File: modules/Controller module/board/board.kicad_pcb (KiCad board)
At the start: 2 copper layers, 60 parts, among them IC1 DW01A, J1 USB_C_Receptacle, J2 Conn_01x05_Female, J3 Conn_01x03_Female, J4 Conn_01x04_Female, J5 Conn_02x12_Odd_Even, J6 Conn_01x06_Female, J7 Conn_01x02_Female, J8 Conn_01x08_Female, Q1 AO3400A, Q2 AO3401A, Q3 FS8205A, SW1 SW_Push, SW2 SW_Push, U1 HT7833, U2 ESP32-WROOM-32D, U3 TP4056, U4 MPU-6050

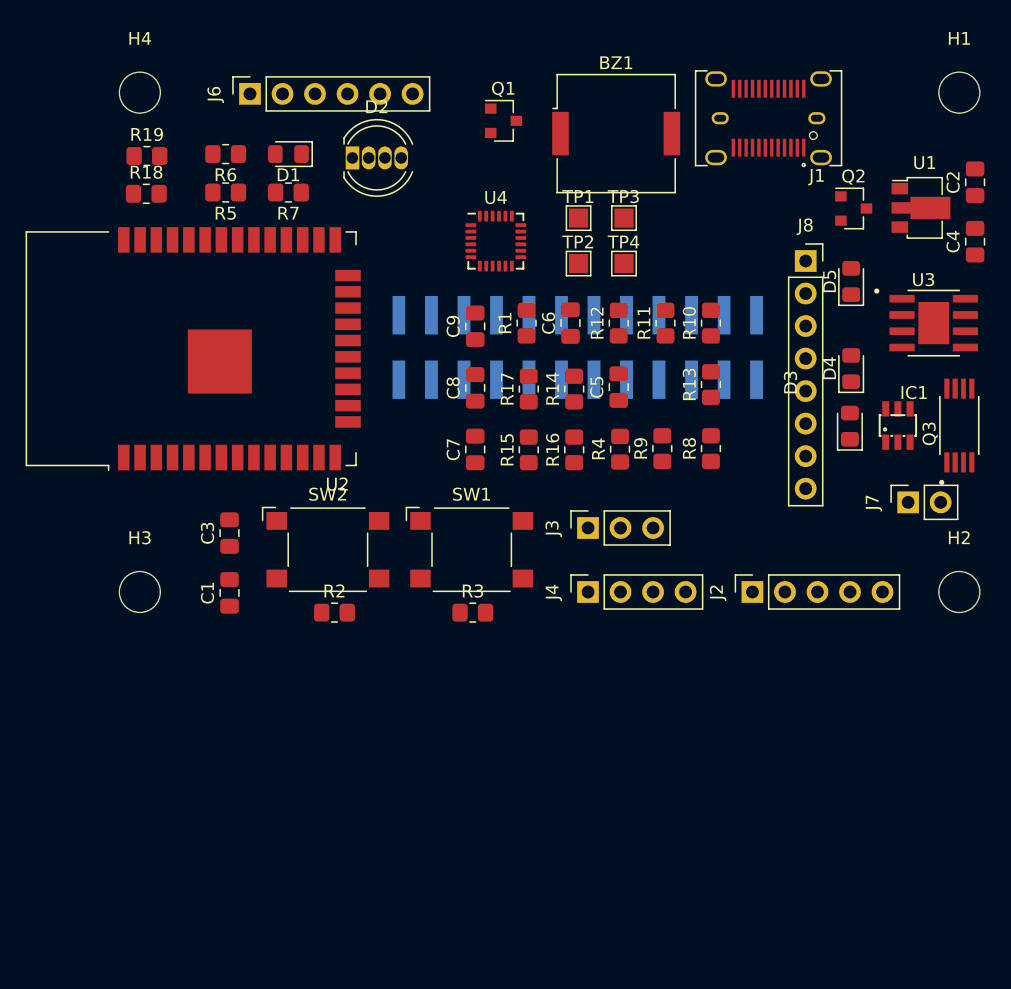
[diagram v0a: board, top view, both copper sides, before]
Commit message: Controller module: Schematic and PCB layout
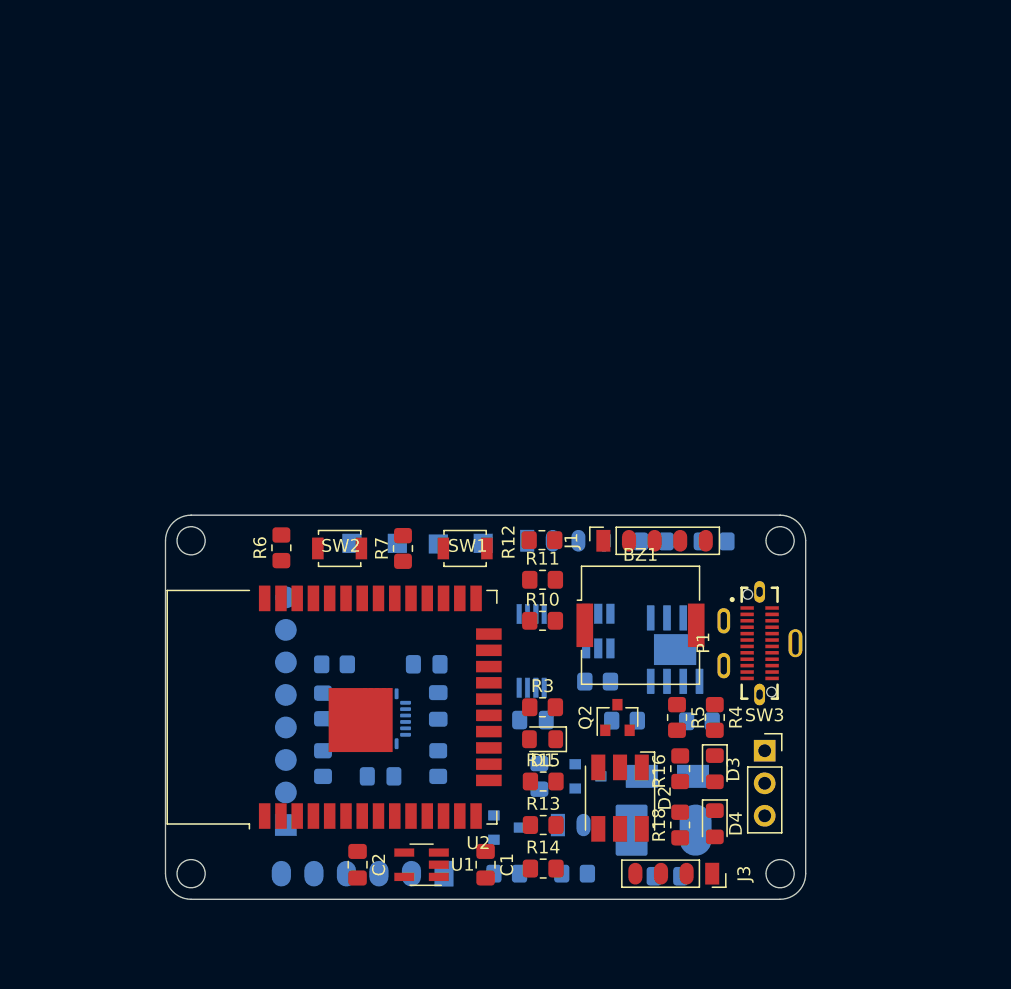
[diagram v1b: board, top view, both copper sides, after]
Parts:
- removed the C1 at (110.0, 92.1)
- removed the C3 at (110.0, 87.4)
- removed the J1 at (152.1, 55.0)
- removed the J3 at (138.0, 87.0)
- removed the J5 at (137.2, 72.9)
- added J2: Conn_01x04_Female, Board:SolderWire_1x04_P2.00mm, B.Cu at (133.2, 88.0)
- added J4: Conn_01x02, Board:SolderWire_1x02_P2.00mm, B.Cu at (135.7, 110.2)
- added P1: USB_C_Plug_USB2.0, Board:GCT_USB4151-GF-C_REVA, F.Cu at (151.4, 96.0)
- added Q2: AO3400A, Package_TO_SOT_SMD:SOT-23, F.Cu at (140.3, 101.8)
- added R1: 10k, Resistor_SMD:R_0805_2012Metric_Pad1.20x1.40mm_HandSolder, B.Cu at (143.1, 88.0)
- added R2: 10k, Resistor_SMD:R_0805_2012Metric_Pad1.20x1.40mm_HandSolder, B.Cu at (147.8, 88.0)
- added R4: 100R, Resistor_SMD:R_0805_2012Metric_Pad1.20x1.40mm_HandSolder, F.Cu at (147.9, 101.8)
- added R5: 10k, Resistor_SMD:R_0805_2012Metric_Pad1.20x1.40mm_HandSolder, F.Cu at (144.9, 101.8)
- added R8: 100R, Resistor_SMD:R_0805_2012Metric_Pad1.20x1.40mm_HandSolder, B.Cu at (136.9, 114.0)
- added R9: 10k, Resistor_SMD:R_0805_2012Metric_Pad1.20x1.40mm_HandSolder, B.Cu at (131.7, 114.0)
- added SW3: SW_SPST, Connector_PinSocket_2.54mm:PinSocket_1x03_P2.54mm_Vertical, F.Cu at (151.8, 104.4)
- C1: renamed from C2; value 1uF -> 10uF
- C2: renamed from C4; value 2.2uF -> 10uF
- C3: renamed from C5; moved to B.Cu
- C4: renamed from C6; moved to B.Cu
- C5: renamed from C7; moved to B.Cu
- C6: renamed from C8; moved to B.Cu
- C7: renamed from C9; moved to B.Cu
- D2: value LED_RGBC -> LED_RGB; footprint LED_THT:LED_D5.0mm-4_RGB -> LED_SMD:LED_RGB_5050-6
- D5: footprint Diode_SMD:D_0805_2012Metric_Pad1.15x1.40mm_HandSolder -> Diode_SMD:D_SMA; moved to B.Cu
- H1, H2, H3, H4: footprint MountingHole:MountingHole_3.2mm_M3 -> MountingHole:MountingHole_2.2mm_M2
- IC1: footprint board:SOT23-6 -> Package_TO_SOT_SMD:SOT-23-6_Handsoldering; moved to B.Cu
- J1: renamed from J2; footprint Connector_PinSocket_2.54mm:PinSocket_1x05_P2.54mm_Vertical -> Board:SolderWire_1x05_P2.00mm
- J3: renamed from J4; footprint Connector_PinSocket_2.54mm:PinSocket_1x04_P2.54mm_Vertical -> Board:SolderWire_1x04_P2.00mm
- J5: renamed from J6; footprint Connector_PinSocket_2.54mm:PinSocket_1x06_P2.54mm_Vertical -> Board:SolderWire_1x06_P2.54mm; moved to B.Cu
- J6: renamed from J7; footprint Connector_PinSocket_2.54mm:PinSocket_1x02_P2.54mm_Vertical -> Board:SolderWire-SMD-BATT; moved to B.Cu
- J7: renamed from J8; footprint Connector_PinSocket_2.54mm:PinSocket_1x08_P2.54mm_Vertical -> Board:MPU6050_Breakout; moved to B.Cu
- Q1, TP1, TP2, TP3, TP4, U4: moved to B.Cu
- Q3: renamed from Q2; moved to B.Cu
- Q4: renamed from Q3; footprint board:SOP65P640X120-8N -> Board:SOP65P640X120-8N; moved to B.Cu
- R17: renamed from R9; moved to B.Cu
- R19: renamed from R11; moved to B.Cu
- R20: renamed from R12; moved to B.Cu
- R21: renamed from R13; moved to B.Cu
- R22: renamed from R14; moved to B.Cu
- R23: renamed from R15; moved to B.Cu
- R24: renamed from R16; moved to B.Cu
- R25: renamed from R17; moved to B.Cu
- SW1, SW2: footprint Button_Switch_SMD:SW_SPST_Omron_B3FS-100xP -> Button_Switch_SMD:SW_SPST_B3U-1000P
- U1: value HT7833 -> ME6211; footprint Package_TO_SOT_SMD:SOT-89-3 -> Package_TO_SOT_SMD:SOT-23-5_HandSoldering
- U3: footprint board:SOP127P600X175-9N -> Board:SOP127P600X175-9N; moved to B.Cu
- moved C2 68.5 mm to (120.0, 113.3), turned to 270 degrees
- moved C1 65.6 mm to (130.0, 113.3), turned to 270 degrees
- moved U1 64.4 mm to (125.0, 113.3), turned to 180 degrees
- moved J5 62.8 mm to (126.8, 114.0)
- moved R14 61.1 mm to (134.5, 113.6), turned to 0 degrees
- moved J7 59.7 mm to (114.5, 110.0)
- moved R13 55.3 mm to (134.5, 110.2), turned to 0 degrees
- moved Q1 55.2 mm to (131.7, 110.4)
- moved D2 54.2 mm to (140.5, 108.1), turned to 270 degrees
- moved R15 50.1 mm to (134.5, 106.8), turned to 0 degrees
- moved D1 49.8 mm to (134.4, 103.5)
- moved Q3 49.0 mm to (138.0, 106.4)
- moved C4 43.9 mm to (144.2, 114.2), turned to 0 degrees
- moved R11 43.2 mm to (134.4, 91.0)
- moved R12 43.0 mm to (134.4, 88.0)
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- renumbered R4 to R10, R18 to R11, R19 to R12, R5 to R13, R6 to R14, R7 to R15, R8 to R16, R10 to R18, R1 to R3, R2 to R6, R3 to R7
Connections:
- C1 pad 2: Net-(C2-Pad2) -> GND
- C2 pad 2: Net-(C2-Pad2) -> GND
- D2 pad 1: Net-(D2-Pad1) -> GND
- D2 pad 2: Net-(D2-Pad2) -> GND
- D2 pad 3: Net-(D2-Pad3) -> GND
- D2 pad 4: GND -> Net-(D2-Pad4)
- Q1 pad 1: /BUZZER -> Net-(Q1-Pad1)
- R13 pad 2: Net-(D2-Pad3) -> Net-(D2-Pad4)
- R14 pad 2: Net-(D2-Pad2) -> Net-(D2-Pad5)
- R15 pad 2: Net-(D2-Pad1) -> Net-(D2-Pad6)
- U1 pad 1: GND -> VCC
- U1 pad 2: VCC -> GND
- U1 pad 3: +3V3 -> VCC
- U2 pad 23: /IO15 -> (no net)
- U2 pad 29: /IO5 -> (no net)
- U2 pad 37: /IO23 -> /BTN-C
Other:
- board outline added: 50 x 30 mm

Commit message: Controller module: PCB complete
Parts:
- removed TP1, TP2, TP3, TP4: TestPoint, TestPoint:TestPoint_Pad_1.5x1.5mm
- added D2: LED, LED_SMD:LED_0805_2012Metric_Pad1.15x1.40mm_HandSolder, F.Cu at (130.0, 113.2)
- added R6: 10k, Resistor_SMD:R_0805_2012Metric_Pad1.20x1.40mm_HandSolder, F.Cu at (127.3, 113.2)
- J6: footprint Board:SolderWire-SMD-BATT -> Board:SolderWire_1x02_P2.00mm
- U2: footprint RF_Module:ESP32-WROOM-32 -> Board:ESP32-WROOM-32
- moved C4 23.4 mm to (144.7, 90.8)
- moved R1 23.1 mm to (120.0, 88.2)
- moved R2 23.1 mm to (124.8, 88.2)
- moved J6 23.0 mm to (145.7, 88.0), turned to 90 degrees
- moved R3 17.3 mm to (122.2, 113.2), turned to 90 degrees
- moved C1 16.5 mm to (134.5, 97.4), turned to 0 degrees
- moved C2 16.4 mm to (134.5, 105.7), turned to 0 degrees
- moved U1 15.1 mm to (134.5, 101.6), turned to 270 degrees
- moved D1 13.8 mm to (124.7, 113.2), turned to 270 degrees
- moved R10 11.9 mm to (143.4, 112.0), turned to 90 degrees
- moved R9 9.46 mm to (146.2, 112.0), turned to 270 degrees
- moved Q1 8.11 mm to (139.6, 112.0), turned to 180 degrees
- moved J4 2.11 mm to (135.8, 112.3), turned to 90 degrees
- moved R20 2.10 mm to (138.8, 102.0)
- moved R16 2.00 mm to (134.5, 108.8)
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- renumbered D2 to D3, D3 to D4, D4 to D5, D5 to D6, R9 to R10, R10 to R11, R11 to R12, R12 to R13, R13 to R14, R14 to R15, R15 to R16, R16 to R17, R17 to R18, R18 to R19, R19 to R20, R20 to R21, R21 to R22, R22 to R23, R23 to R24, R24 to R25, R25 to R26, R6 to R7, R7 to R8, R8 to R9, SW3 to SW2, SW2 to SW3
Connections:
- J7 pad 1: +3V3 -> VCC
- U2 pad 23: (no net) -> /IO15
- U2 pad 29: (no net) -> /IO15
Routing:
- net GND: track 0.00 -> 267.3 mm, vias 0 -> 12
- net +3V3: track 0.00 -> 153.9 mm, vias 0 -> 4
- net +5V: track 0.00 -> 70.2 mm, vias 0 -> 1
- net VCC: track 0.00 -> 64.0 mm, vias 0 -> 1
- net /IO16: track 0.00 -> 61.4 mm, vias 0 -> 1
- net /IO15: track 0.00 -> 60.4 mm, vias 0 -> 2
- net /BUZZER: track 0.00 -> 52.8 mm, vias 0 -> 2
- net /BTN2: track 0.00 -> 50.9 mm, vias 0 -> 3
- net /EN: track 0.00 -> 47.1 mm, vias 0 -> 2
- net /BTN1: track 0.00 -> 45.1 mm, vias 0 -> 2
- net /TX: track 0.00 -> 43.9 mm, vias 0 -> 1
- net /BTN-C: track 0.00 -> 41.4 mm, vias 0 -> 1
- net /BTN4: track 0.00 -> 37.9 mm, vias 0 -> 2
- net /BTN3: track 0.00 -> 35.9 mm, vias 0 -> 2
- net Net-(BZ1-Pad1): track 0.00 -> 35.3 mm, vias 0 -> 1
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- added copper zone on B.Cu, net GND
- added copper zone on F.Cu, net GND
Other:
- net class Default: trace_width 0.25 -> 0.2

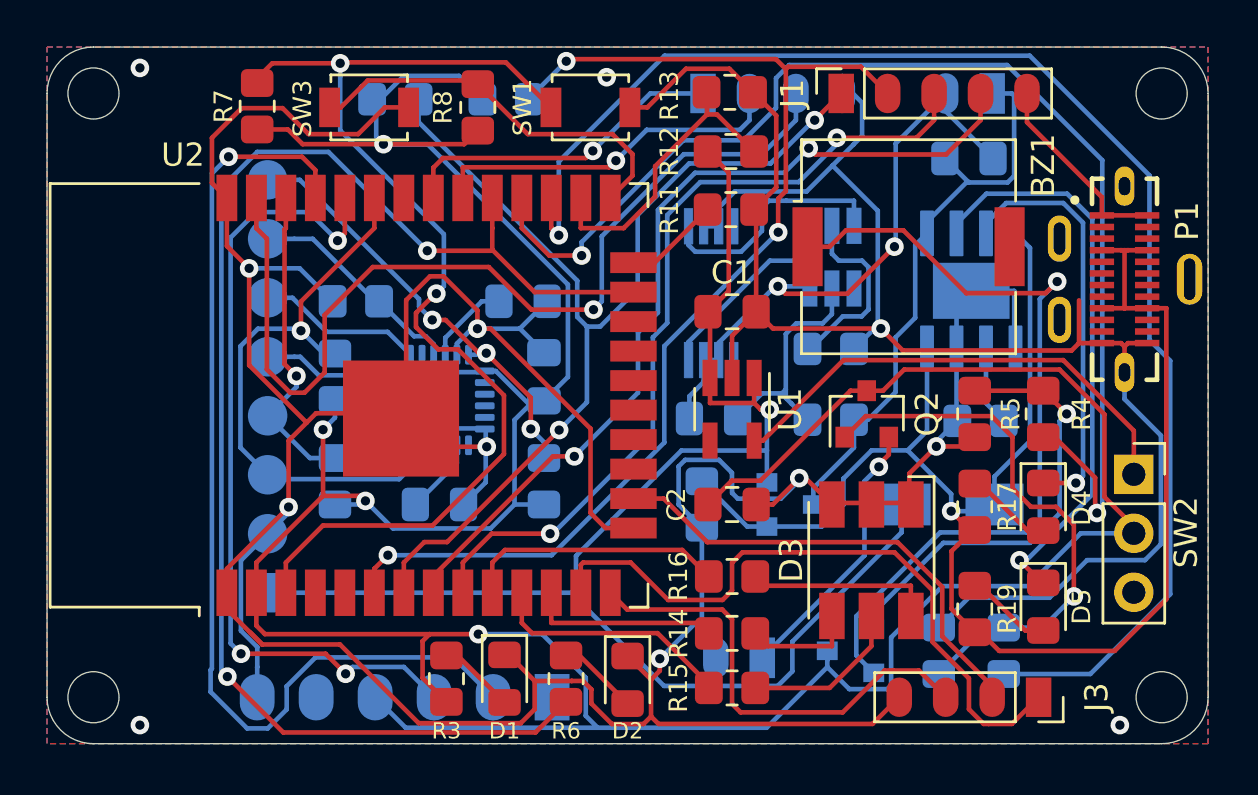
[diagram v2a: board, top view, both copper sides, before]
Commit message: Controller module: PCB modular
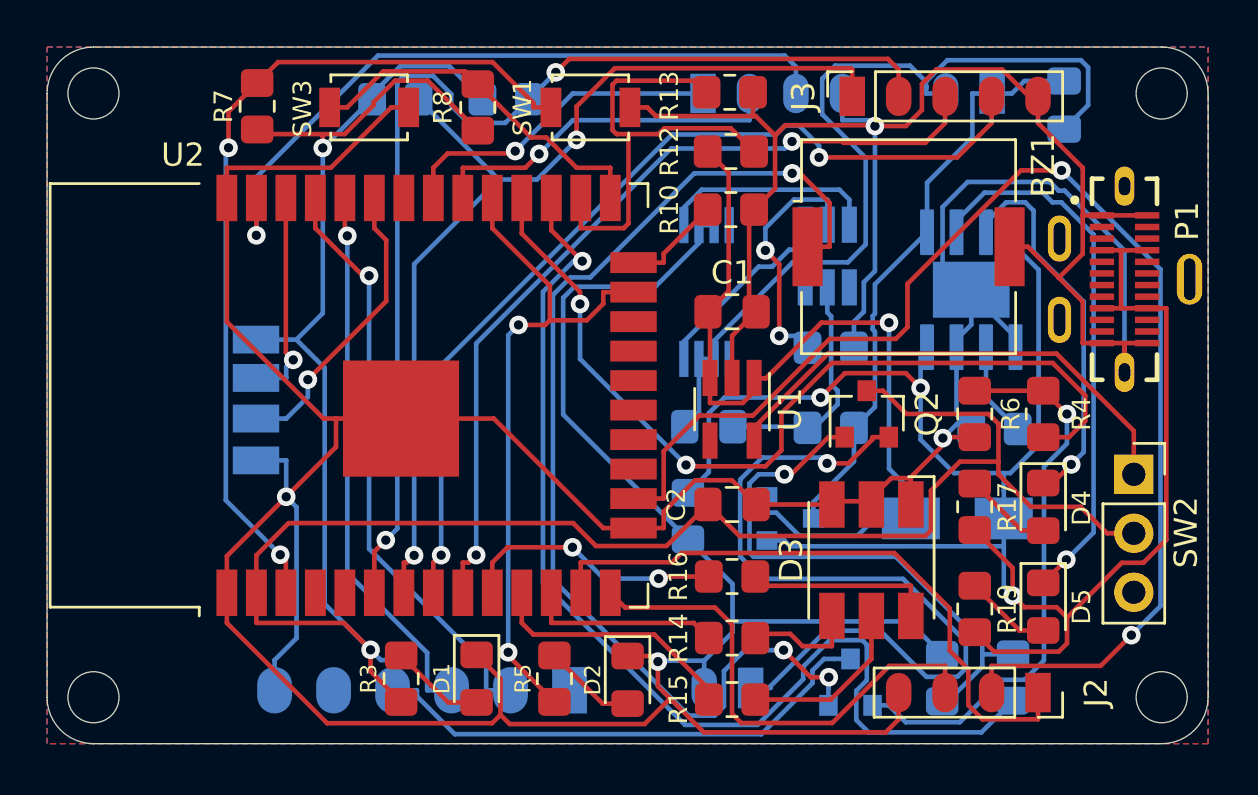
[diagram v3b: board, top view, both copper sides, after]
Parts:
- removed C5, C6: 0.1uF, Capacitor_SMD:C_0805_2012Metric_Pad1.18x1.45mm_HandSolder
- removed C7: 2.2nF, Capacitor_SMD:C_0805_2012Metric_Pad1.18x1.45mm_HandSolder
- removed J7: Conn_01x08_Female, Board:MPU6050_Breakout
- removed R23, R25, R26: 10k, Resistor_SMD:R_0805_2012Metric_Pad1.20x1.40mm_HandSolder
- removed R24: 4.7k, Resistor_SMD:R_0805_2012Metric_Pad1.20x1.40mm_HandSolder
- removed the U4 at (121.9, 101.2)
- added U3: Inertial_Measurement_Unit, Board:Inertial_Measurement_Unit_Board, B.Cu at (121.5, 101.1)
- moved C4 4.70 mm to (148.8, 88.5), turned to 270 degrees
- moved R3 1.95 mm to (120.2, 113.2)
- moved J4 1.39 mm to (135.3, 113.6)
- moved Q1 1.35 mm to (139.6, 113.3), turned to 90 degrees
- moved R9 1.22 mm to (146.6, 113.2)
- moved D1 1.20 mm to (123.5, 113.2)
- moved R11 1.18 mm to (143.6, 113.2)
- moved J5 0.81 mm to (127.5, 113.7)
- moved R18 0.78 mm to (132.6, 106.2)
- moved D6 0.72 mm to (144.2, 106.3)
- moved R20 0.69 mm to (145.8, 102.5)
- moved Q3 0.60 mm to (137.0, 106.3)
- moved R15 0.50 mm to (134.5, 114.1)
- moved R5 0.50 mm to (126.8, 113.2)
- moved J3 0.49 mm to (139.7, 88.1)
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- renumbered J2 to J1, J3 to J2, J1 to J3, R11 to R10, R10 to R11, R21 to R20, R20 to R21, R6 to R5, R5 to R6, U3 to U4
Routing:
- net /BTN-M: track 21.2 -> 56.6 mm, vias 0 -> 2
- net /IO15: track 60.4 -> 29.4 mm
- net VCC: track 64.0 -> 37.5 mm
- net Net-(J4-Pad1): track 11.8 -> 34.4 mm
- net +3V3: track 153.9 -> 134.0 mm, vias 4 -> 2
- net /IMU/INT: track 19.0 -> 0.00 mm, vias 3 -> 0
- net /TX: track 43.9 -> 25.5 mm
- net /BUZZER: track 52.8 -> 38.2 mm
- net /IO16: track 61.4 -> 47.4 mm
- net +5V: track 70.2 -> 84.2 mm, vias 1 -> 3
- net /IO21: track 25.5 -> 12.8 mm
- net Net-(BZ1-Pad1): track 35.3 -> 47.8 mm, vias 1 -> 3
- net GND: track 267.3 -> 255.4 mm, vias 12 -> 4
- net /BMS/BATT-: track 27.1 -> 38.8 mm, vias 2 -> 0
- net /RX: track 35.0 -> 23.7 mm, vias 3 -> 1
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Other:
- board text added: "InputBlackBoxOutput"
